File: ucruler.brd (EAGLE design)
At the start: 200 x 32 mm, 58 parts

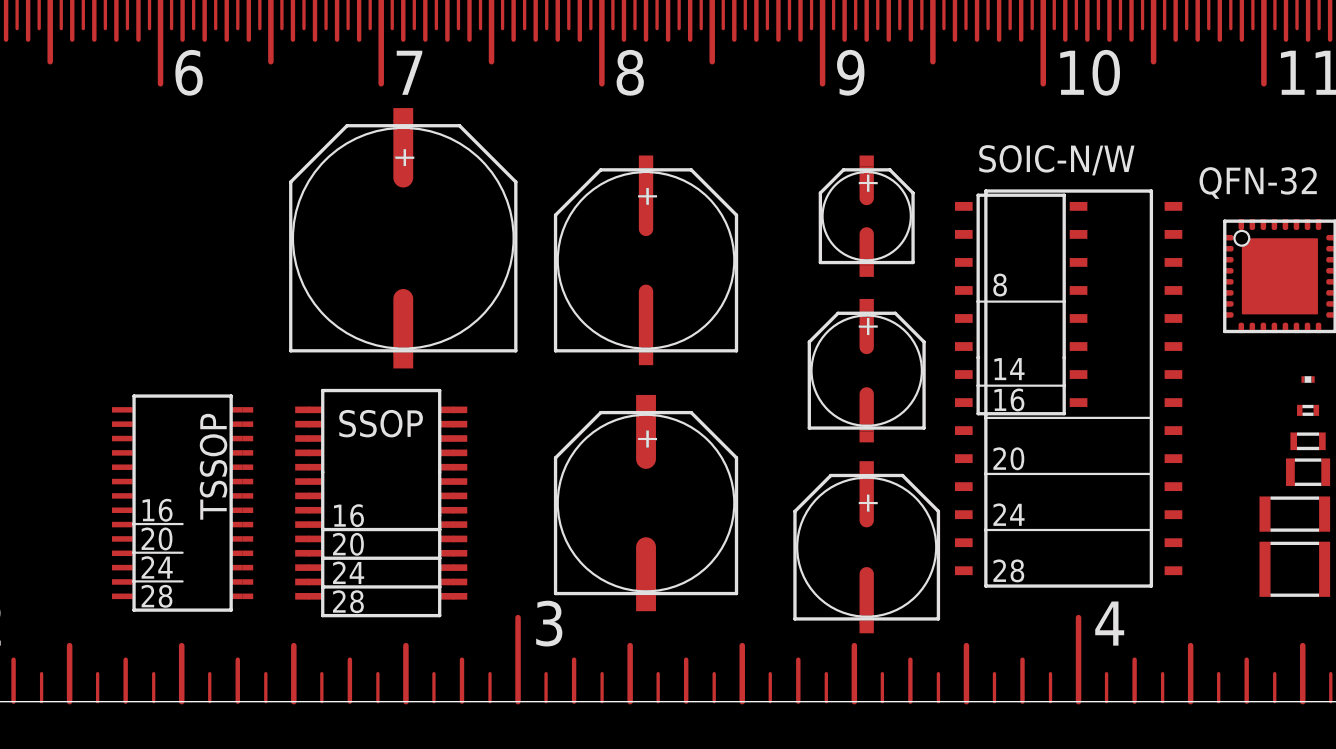
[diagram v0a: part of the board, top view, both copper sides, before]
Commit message: redesign multiple pin count packages
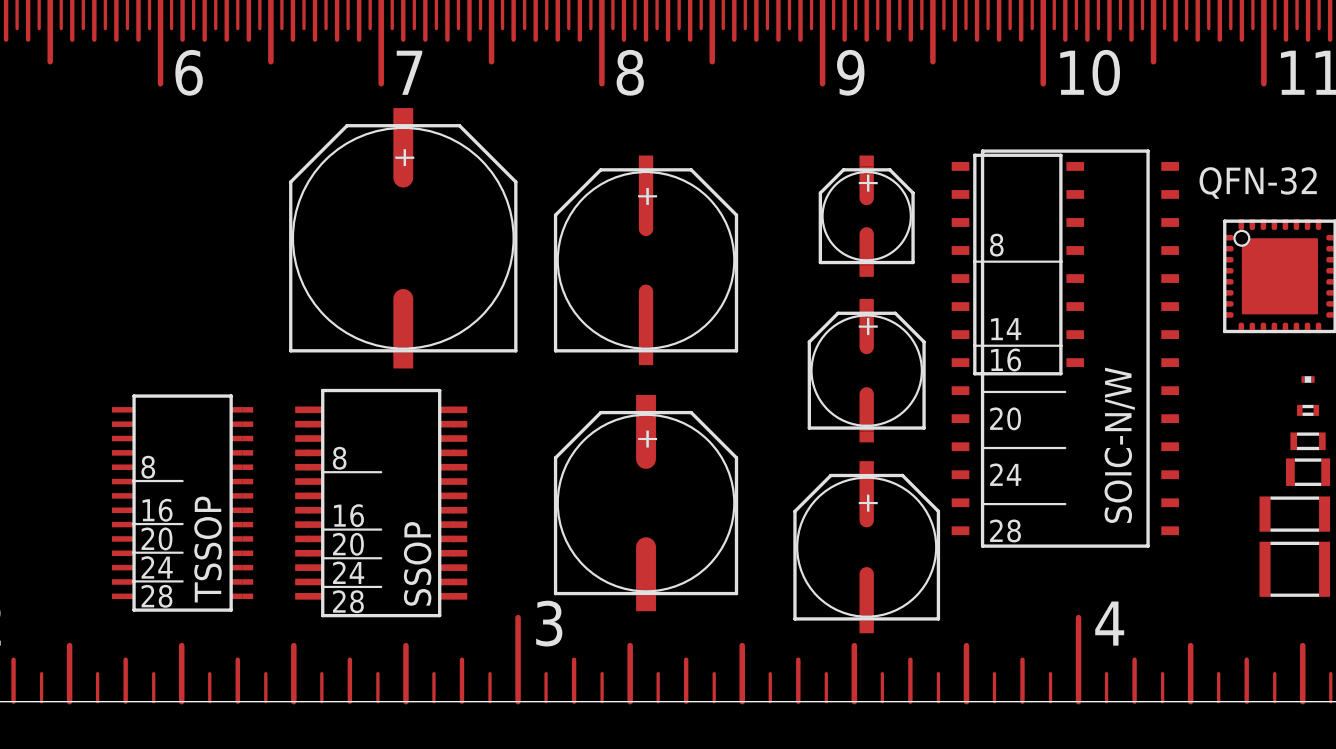
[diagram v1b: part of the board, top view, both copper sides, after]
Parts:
- moved E$47 5.39 mm to (101.0, 16.0)
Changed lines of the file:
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@@
 <text x="120" y="15" size="1.2" layer="21" ratio="10" distance="20">PLCC-4</text>
 <text x="120" y="10" size="1.2" layer="21" ratio="10" distance="20">PLCC-6</text>
-<text x="97" y="24" size="1.2" layer="21" ratio="10" distance="20">SOIC-N/W</text>
+<text x="104" y="8" size="1.2" layer="21" ratio="10" distance="20" rot="R90">SOIC-N/W</text>
 <text x="107" y="23" size="1.2" layer="21" ratio="10" distance="20">QFN-32</text>
 <text x="128.5" y="14.75" size="1.2" layer="21" ratio="10" distance="20" rot="R90">SOD323/SC76</text>
 <text x="137.25" y="15.5" size="1.2" layer="21" ratio="10" distance="20" rot="R90">SC79</text>
-<text x="68" y="12" size="1.2" layer="21" ratio="10" distance="20">SSOP</text>
-<text x="63" y="8.25" size="1.2" layer="21" ratio="10" distance="20" rot="R90">TSSOP</text>
+<text x="72.25" y="4.25" size="1.2" layer="21" ratio="10" distance="20" rot="R90">SSOP</text>
+<text x="62.75" y="4.5" size="1.2" layer="21" ratio="10" distance="20" rot="R90">TSSOP</text>
 </plain>
 <attributes>
@@
 <element name="E$45" library="ucruler" package="PACK-1206" value="" x="111.4" y="8.5"/>
 <element name="E$46" library="ucruler" package="PACK-1210" value="" x="111.4" y="6"/>
-<element name="E$47" library="ucruler" package="PACK-SOIC" value="" x="96" y="18"/>
+<element name="E$47" library="ucruler" package="PACK-SOIC" value="" x="101" y="16"/>
 <element name="E$48" library="ucruler" package="PACK-QFN-32" value="" x="109" y="21"/>
 <element name="E$49" library="ucruler" package="PACK-SOD323" value="" x="128" y="13"/>

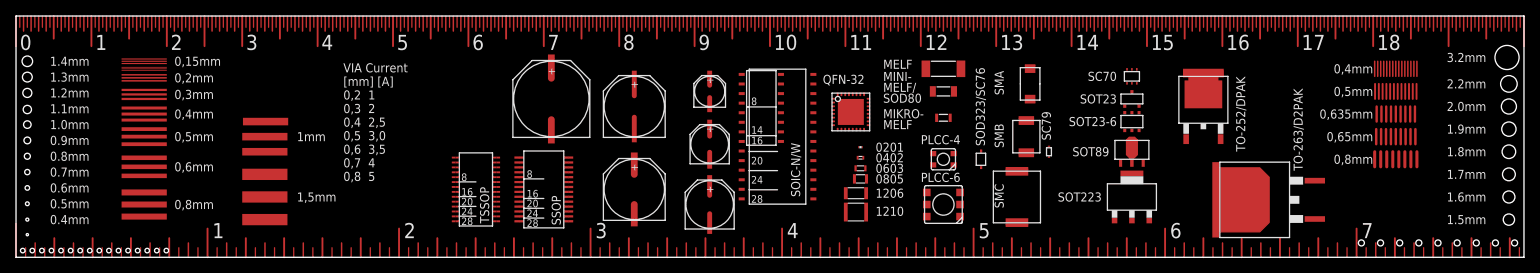
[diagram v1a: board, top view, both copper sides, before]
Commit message: pin space gauge/counting helper
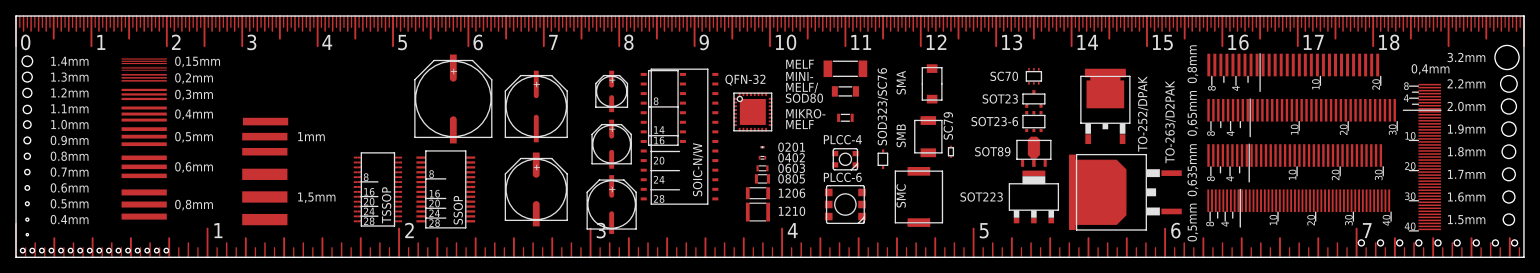
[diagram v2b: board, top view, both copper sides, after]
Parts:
- removed E$8: (no value), ucruler:PINSPACE-0,8-C6
- added E$59: (no value), ucruler:PINCOUNT-0.4
- E$10: device ucruler:PINSPACE-0,635-C6 -> ucruler:PINCOUNT-0,65
- E$6: device ucruler:PINSPACE-0,4-C6 -> ucruler:PINCOUNT-0,5
- E$7: device ucruler:PINSPACE-0,5-C6 -> ucruler:PINCOUNT-0,635
- E$9: device ucruler:PINSPACE-0,65-C6 -> ucruler:PINCOUNT-0,8
- moved E$6 31.4 mm to (158.0, 6.00), turned to 90 degrees
- moved E$7 26.9 mm to (158.0, 12.0), turned to 90 degrees
- moved E$9 26.2 mm to (158.0, 24.0), turned to 90 degrees
- moved E$10 25.0 mm to (158.0, 18.0), turned to 90 degrees
- moved E$32 19.0 mm to (149.9, 8.62)
- moved E$15 13.0 mm to (135.0, 24.0)
- moved E$16 13.0 mm to (135.0, 21.0)
- moved E$17 13.0 mm to (135.0, 18.0)
- moved E$18 13.0 mm to (135.0, 14.0)
- moved E$19 13.0 mm to (135.0, 8.00)
- moved E$31 13.0 mm to (144.5, 17.8)
- moved E$33 13.0 mm to (121.0, 16.0)
- moved E$34 13.0 mm to (119.8, 8.00)
- moved E$35 13.0 mm to (121.5, 23.0)
- moved E$36 13.0 mm to (110.0, 25.0)
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
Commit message: rearranged complete front
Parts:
- added E$60: (no value), ucruler:COPPER-FONT
- added E$8: (no value), ucruler:COPPER-FONT-INV
- moved E$15 90.0 mm to (45.0, 25.0), turned to 90 degrees
- moved E$32 89.9 mm to (60.0, 8.00), turned to 0 degrees
- moved E$17 79.1 mm to (56.2, 25.0)
- moved E$18 78.3 mm to (57.0, 21.0)
- moved E$31 74.3 mm to (71.0, 7.00)
- moved E$16 73.8 mm to (61.2, 23.0)
- moved E$48 70.4 mm to (25.8, 25.0)
- moved E$19 64.9 mm to (71.0, 19.0)
- moved E$47 40.0 mm to (48.0, 14.0)
- moved E$56 27.3 mm to (83.0, 10.0)
- moved E$54 26.4 mm to (93.0, 9.00)
- moved E$55 26.4 mm to (93.0, 20.0)
- moved E$41 22.8 mm to (79.0, 25.6)
- moved E$42 22.8 mm to (79.0, 24.2)
- moved E$43 22.8 mm to (79.0, 22.8)
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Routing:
- added copper zone on layer 1, net S$16
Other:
- board text added: "0,1mm"
- board text added: "B"
- board text added: "C"
- board text added: "D/D8"
- board text added: "E"
- board text added: "F"
- board text added: "G"
- board text added: "MikroMELF"
- board text added: "MiniMELF SOD80"
- board text added: "SOD323 SC76"
- board text added: "Your AD HERE!"
- board text removed: "MIKRO- MELF"
- board text removed: "MINI- MELF/ SOD80"
- board text removed: "SOD323/SC76"

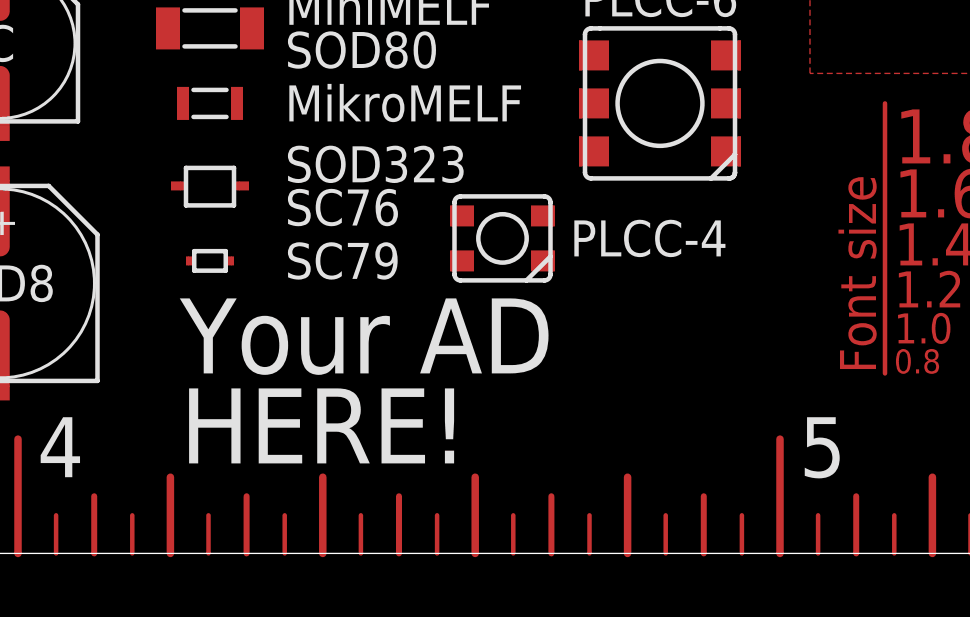
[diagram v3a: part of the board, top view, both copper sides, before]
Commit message: spacing cap e/f; plcc aligned
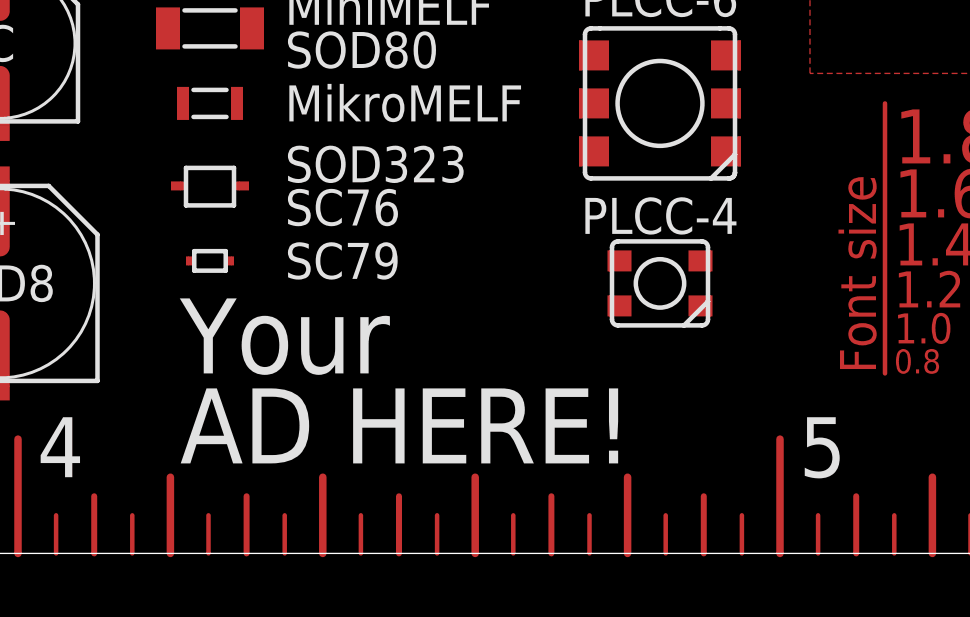
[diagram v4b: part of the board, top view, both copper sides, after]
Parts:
- moved E$39 5.46 mm to (123.0, 9.00)
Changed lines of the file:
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@@
 SOD80</text>
 <text x="110.5" y="15" size="1.2" layer="21" ratio="13" distance="20" align="center-left">MikroMELF</text>
-<text x="120" y="10.5" size="1.2" layer="21" ratio="13" distance="20" align="center-left">PLCC-4</text>
+<text x="123" y="11.25" size="1.2" layer="21" ratio="13" distance="20" align="center">PLCC-4</text>
 <text x="123" y="18.5" size="1.2" layer="21" ratio="13" distance="20" align="center">PLCC-6</text>
 <text x="51.25" y="14.25" size="1.2" layer="21" ratio="13" distance="20" rot="R90">SOIC-N/W</text>
@@
 <rectangle x1="148" y1="6" x2="150.5" y2="26" layer="29"/>
 <rectangle x1="153" y1="6" x2="154.25" y2="26" layer="29"/>
-<text x="107" y="3" size="2.5" layer="21" ratio="13" distance="20">Your AD
-HERE!</text>
+<text x="107" y="3" size="2.5" layer="21" ratio="13" distance="20">Your
+AD HERE!</text>
 </plain>
 <attributes>
@@
 <element name="E$37" library="ucruler" package="PACK-MELF-MINI" value="" x="108" y="17.5" rot="R270"/>
 <element name="E$38" library="ucruler" package="PACK-MELF-MICRO" value="" x="108" y="15" rot="R270"/>
-<element name="E$39" library="ucruler" package="PACK-PLCC-4" value="" x="117.75" y="10.5" rot="R90"/>
+<element name="E$39" library="ucruler" package="PACK-PLCC-4" value="" x="123" y="9" rot="R90"/>
 <element name="E$40" library="ucruler" package="PACK-PLCC-6" value="" x="123" y="15" rot="R90"/>
 <element name="E$41" library="ucruler" package="PACK-0201" value="" x="79" y="25.6" rot="R180"/>

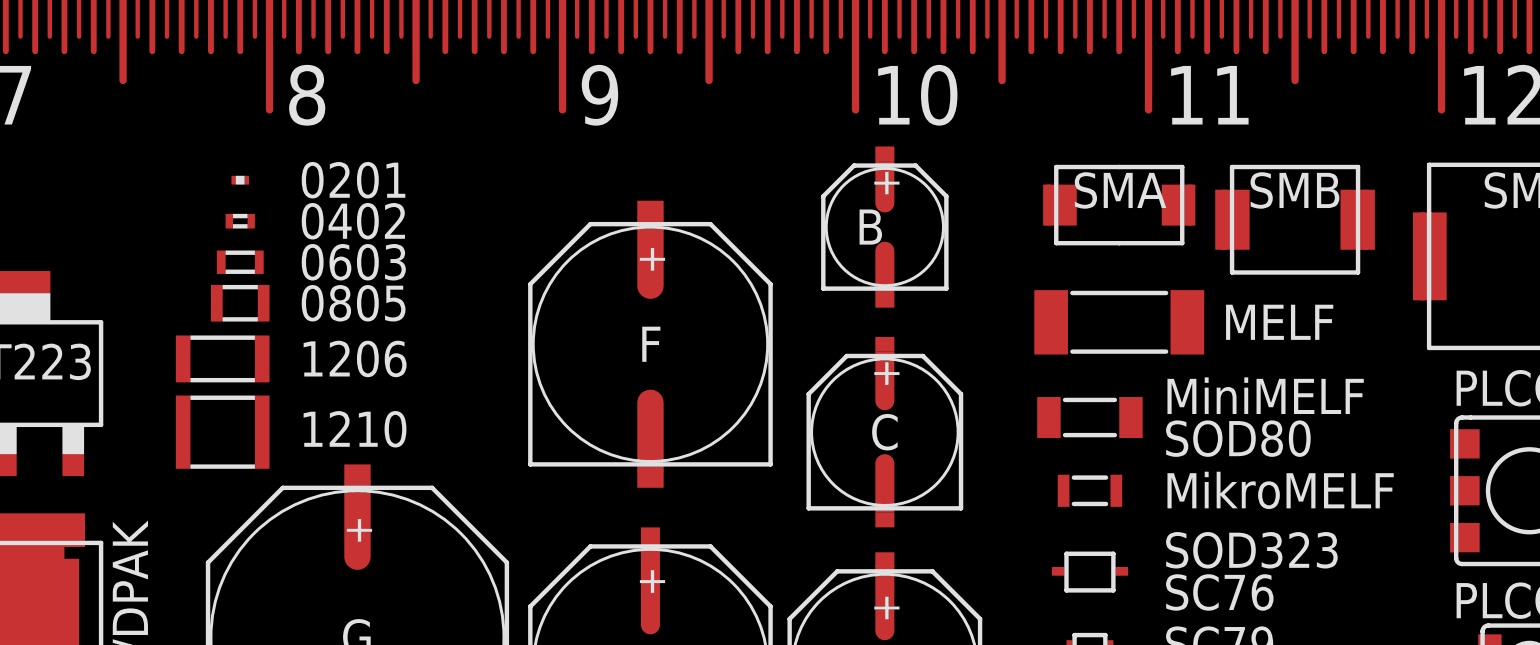
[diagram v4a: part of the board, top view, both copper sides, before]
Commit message: fixed polygon with for 4 packages
PACK-SOT89
PACK-TO252
PACK-PLCC-4
PACK-QFN-32
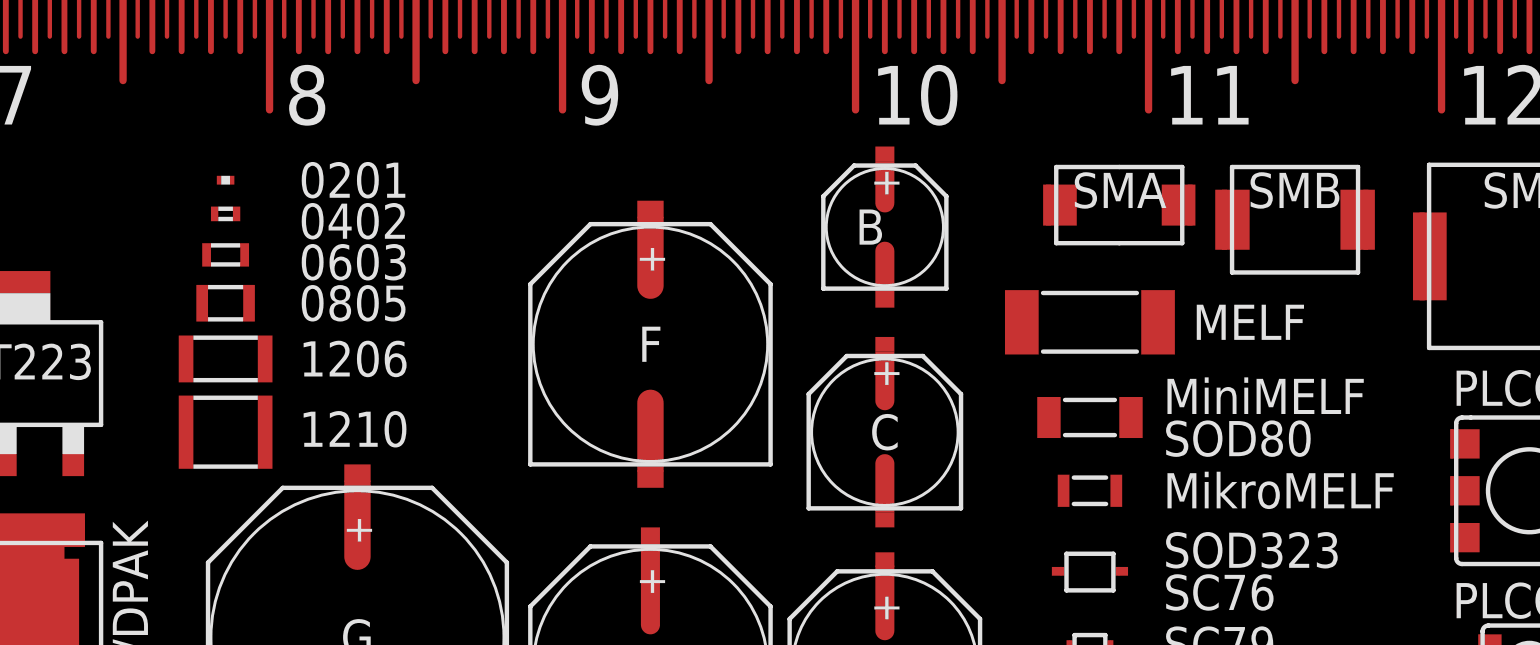
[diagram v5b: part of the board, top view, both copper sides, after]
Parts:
- moved E$36 1.00 mm to (108.0, 20.8)
- moved E$42 0.56 mm to (78.5, 24.4)
- moved E$43 0.56 mm to (78.5, 23.1)
- moved E$41 0.50 mm to (78.5, 25.6)
- moved E$44 0.50 mm to (78.5, 21.4)
- moved E$45 0.10 mm to (78.5, 19.5)
- moved E$46 0.10 mm to (78.5, 17.0)
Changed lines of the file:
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@@
 <text x="115" y="25.25" size="1.2" layer="21" ratio="13" distance="20" align="center">SMB</text>
 <text x="123" y="25.25" size="1.2" layer="21" ratio="13" distance="20" rot="R180" align="center">SMC</text>
-<text x="112.5" y="20.75" size="1.2" layer="21" ratio="13" distance="20" align="center-left">MELF</text>
+<text x="111.5" y="20.75" size="1.2" layer="21" ratio="13" distance="20" align="center-left">MELF</text>
 <text x="110.5" y="17.5" size="1.2" layer="21" ratio="13" distance="20" align="center-left">MiniMELF
 SOD80</text>
@@
 <element name="E$34" library="ucruler" package="PACK-DO214AB-SMC" value="" x="123" y="23" rot="R270"/>
 <element name="E$35" library="ucruler" package="PACK-DO214AC-SMA" value="" x="109" y="24.75" rot="R270"/>
-<element name="E$36" library="ucruler" package="PACK-MELF" value="" x="109" y="20.75" rot="R90"/>
+<element name="E$36" library="ucruler" package="PACK-MELF" value="" x="108" y="20.75" rot="R90"/>
 <element name="E$37" library="ucruler" package="PACK-MELF-MINI" value="" x="108" y="17.5" rot="R270"/>
 <element name="E$38" library="ucruler" package="PACK-MELF-MICRO" value="" x="108" y="15" rot="R270"/>
 <element name="E$39" library="ucruler" package="PACK-PLCC-4" value="" x="123" y="9" rot="R90"/>
 <element name="E$40" library="ucruler" package="PACK-PLCC-6" value="" x="123" y="15" rot="R90"/>
-<element name="E$41" library="ucruler" package="PACK-0201" value="" x="79" y="25.6" rot="R180"/>
-<element name="E$42" library="ucruler" package="PACK-0402" value="" x="79" y="24.2" rot="R180"/>
-<element name="E$43" library="ucruler" package="PACK-0603" value="" x="79" y="22.8" rot="R180"/>
-<element name="E$44" library="ucruler" package="PACK-0805" value="" x="79" y="21.4" rot="R180"/>
-<element name="E$45" library="ucruler" package="PACK-1206" value="" x="78.4" y="19.5"/>
-<element name="E$46" library="ucruler" package="PACK-1210" value="" x="78.4" y="17"/>
+<element name="E$41" library="ucruler" package="PACK-0201" value="" x="78.5" y="25.6" rot="R180"/>
+<element name="E$42" library="ucruler" package="PACK-0402" value="" x="78.5" y="24.45" rot="R180"/>
+<element name="E$43" library="ucruler" package="PACK-0603" value="" x="78.5" y="23.05" rot="R180"/>
+<element name="E$44" library="ucruler" package="PACK-0805" value="" x="78.5" y="21.4" rot="R180"/>
+<element name="E$45" library="ucruler" package="PACK-1206" value="" x="78.5" y="19.5"/>
+<element name="E$46" library="ucruler" package="PACK-1210" value="" x="78.5" y="17"/>
 <element name="E$47" library="ucruler" package="PACK-SOIC" value="" x="48" y="14"/>
 <element name="E$48" library="ucruler" package="PACK-QFN-32" value="" x="25.75" y="25"/>

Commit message: font cleanup
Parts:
- added E$61: (no value), ucruler:SILK-FONT-INV
- moved E$28 49.0 mm to (82.0, 27.0)
- moved E$29 31.0 mm to (90.0, 29.0)
- moved E$30 8.00 mm to (120.5, 27.0)
- moved E$22 0.50 mm to (141.0, 28.5)
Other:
- board text added: "0.15mm"
- board text added: "0.1mm"
- board text added: "0.2mm"
- board text added: "0.3mm"
- board text added: "0.635mm"
- board text added: "0.65mm"
- board text removed: "0,15mm"
- board text removed: "0,1mm"
- board text removed: "0,2mm"
- board text removed: "0,3mm"
- board text removed: "0,4mm"
- board text removed: "0,5mm"
- board text removed: "0,635mm"
- board text removed: "0,65mm"
- board text removed: "0,6mm"
- board text removed: "0,8mm"
- board text removed: "1,5mm"
